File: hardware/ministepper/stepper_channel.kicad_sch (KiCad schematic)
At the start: 14 parts, among them U1 TMC2130-LA

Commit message: ministepper: 0.1 ohm sense resistor LCSC confirmed (C2974119)
Previously marked TBD — UNI-ROYAL FRL1210FR100TS is a 1210 / 1%
100 mOhm sense resistor, LCSC C2974119, ~15k stock, $0.015. Used on
RSA and RSB in the stepper_channel sub-sheet (standard variant).

The DNP micro variant (0.68 ohm 1210, C3000593) stays unchanged.
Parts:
- RSA, RSB: LCSC TBD -> C2974119; MPN RL1220T-R100-F -> FRL1210FR100TS; Manufacturer Yageo -> UNI-ROYAL
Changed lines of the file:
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@@
 		(property "Datasheet" "~" (at 170 155 0) (effects (font (size 1.27 1.27)) hide))
 		(property "Description" "Sense coil A, 0.1 ohm 1% 1210 (standard)" (at 170 155 0) (effects (font (size 1.27 1.27)) hide))
-		(property "LCSC" "TBD" (at 170 155 0) (effects (font (size 1.27 1.27)) hide))
-		(property "MPN" "RL1220T-R100-F" (at 170 155 0) (effects (font (size 1.27 1.27)) hide))
-		(property "Manufacturer" "Yageo" (at 170 155 0) (effects (font (size 1.27 1.27)) hide))
+		(property "LCSC" "C2974119" (at 170 155 0) (effects (font (size 1.27 1.27)) hide))
+		(property "MPN" "FRL1210FR100TS" (at 170 155 0) (effects (font (size 1.27 1.27)) hide))
+		(property "Manufacturer" "UNI-ROYAL" (at 170 155 0) (effects (font (size 1.27 1.27)) hide))
 		(instances (project "ministepper" (path "/e1d2c3b4-a5f6-7890-abcd-ef9876543210/c3d4e5f6-a7b8-9012-cdef-1234567890ab" (reference "RSA") (unit 1))))
 	)
@@
 		(property "Datasheet" "~" (at 175 155 0) (effects (font (size 1.27 1.27)) hide))
 		(property "Description" "Sense coil B, 0.1 ohm 1% 1210 (standard)" (at 175 155 0) (effects (font (size 1.27 1.27)) hide))
-		(property "LCSC" "TBD" (at 175 155 0) (effects (font (size 1.27 1.27)) hide))
-		(property "MPN" "RL1220T-R100-F" (at 175 155 0) (effects (font (size 1.27 1.27)) hide))
-		(property "Manufacturer" "Yageo" (at 175 155 0) (effects (font (size 1.27 1.27)) hide))
+		(property "LCSC" "C2974119" (at 175 155 0) (effects (font (size 1.27 1.27)) hide))
+		(property "MPN" "FRL1210FR100TS" (at 175 155 0) (effects (font (size 1.27 1.27)) hide))
+		(property "Manufacturer" "UNI-ROYAL" (at 175 155 0) (effects (font (size 1.27 1.27)) hide))
 		(instances (project "ministepper" (path "/e1d2c3b4-a5f6-7890-abcd-ef9876543210/c3d4e5f6-a7b8-9012-cdef-1234567890ab" (reference "RSB") (unit 1))))
 	)

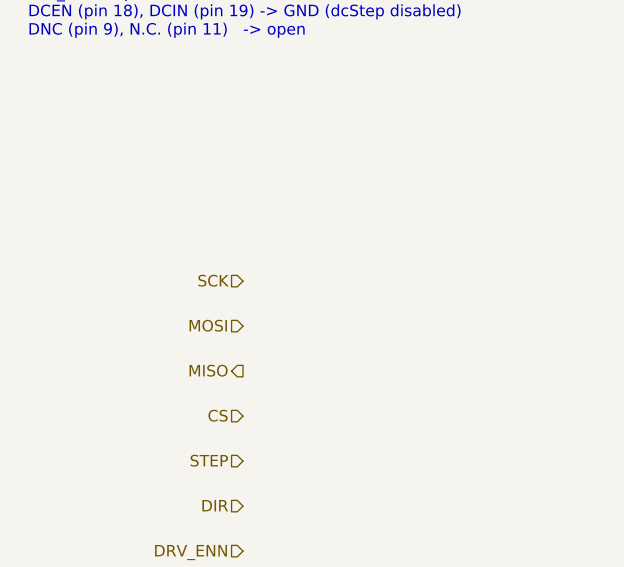
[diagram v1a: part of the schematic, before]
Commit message: ministepper: add (justify left/right) to hier labels and sheet pins
The labels inside stepper_channel.kicad_sch and the sheet-block pins
on the root ministepper.kicad_sch were missing (justify ...) inside
their (effects ...) — which left KiCad to render the text with no
offset from the arrow glyph. User caught it by hand-placing a FOO
hier label in KiCad which came out formatted with (justify left).

Fixed 13 hier labels in the sub-sheet and 24 pins across the two
stepper sheet instances on the root:

  angle 0   (left edge on sub-sheet, or right edge on root sheet) -> justify left
  angle 180 (right edge on sub-sheet, or left edge on root sheet) -> justify right

Text now sits cleanly on the INSIDE side of each pin's triangle glyph
with the standard KiCad offset instead of overlapping the first
letter of each label.
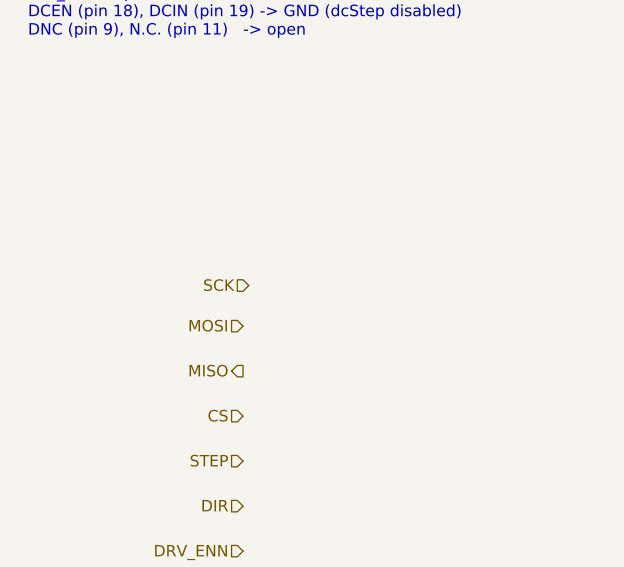
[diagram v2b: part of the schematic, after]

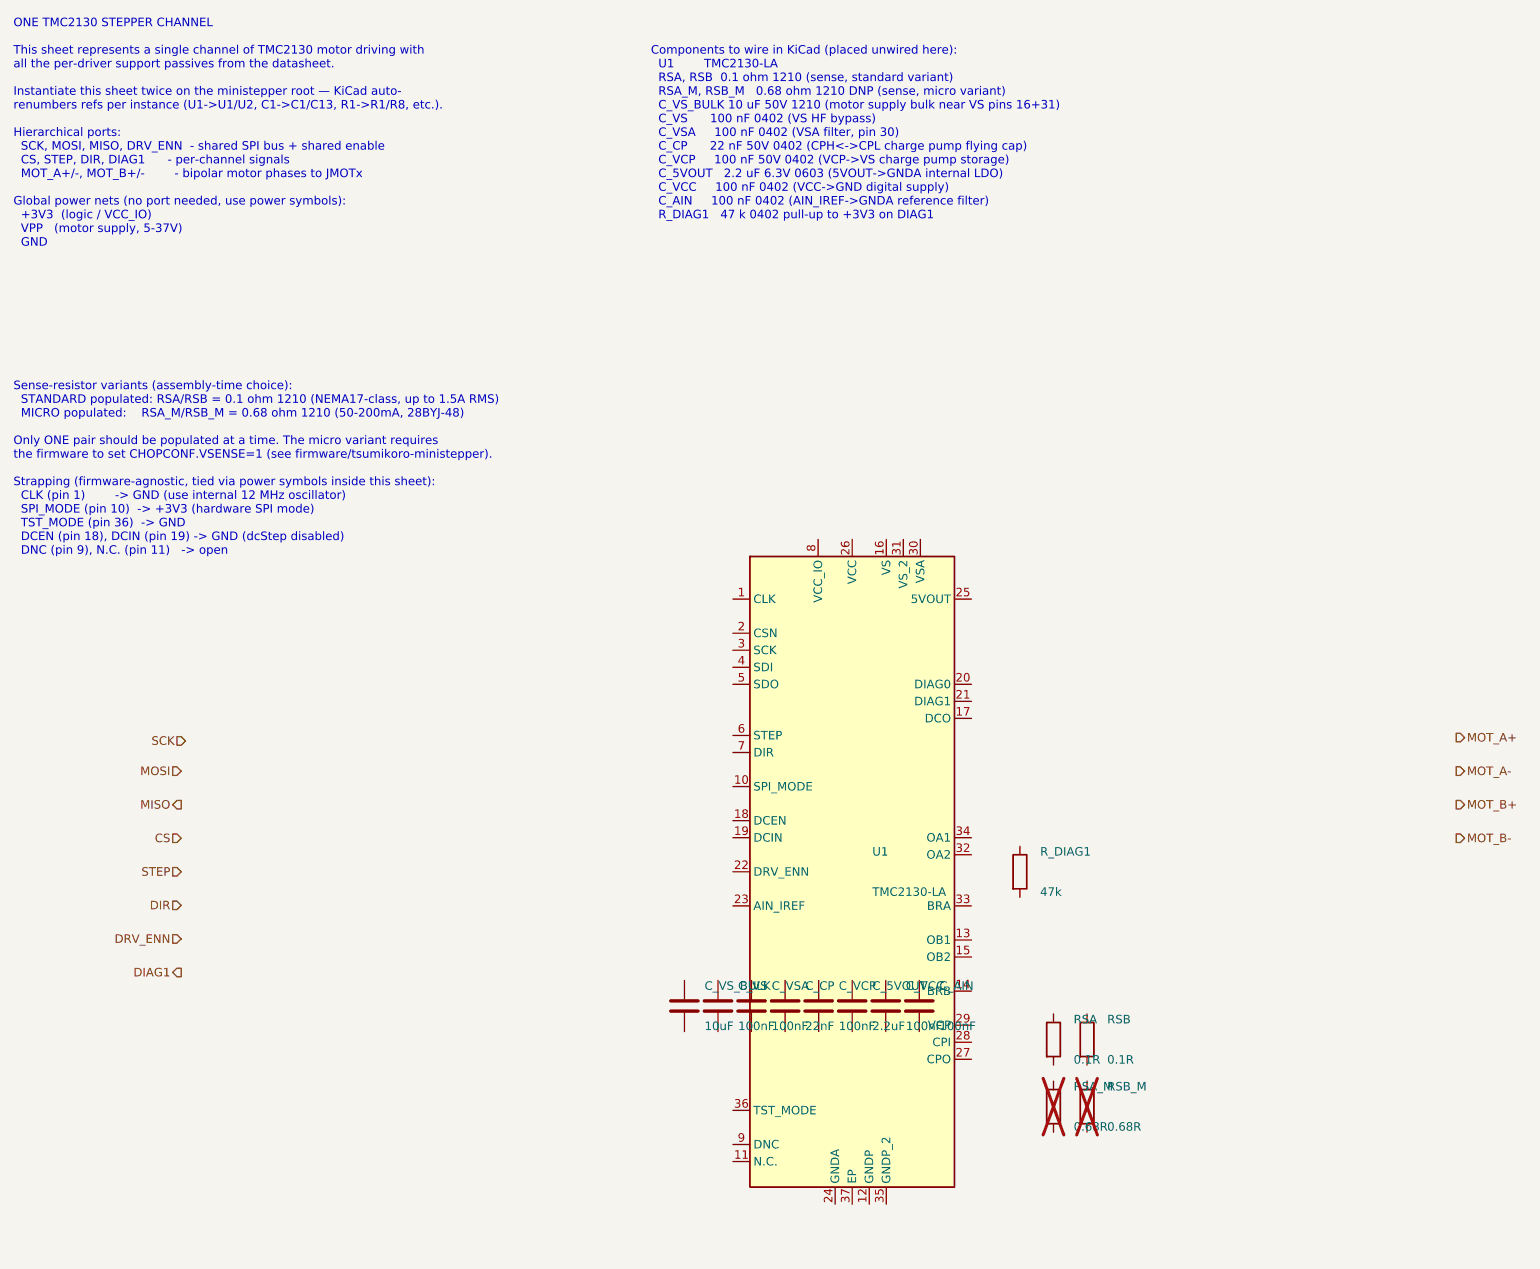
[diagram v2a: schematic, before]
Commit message: ministepper: add BRA/BRB sense-node filter caps
Two new 100 nF 0402 (basic, C1525) caps in stepper_channel.kicad_sch:
  C_BRA_FILT — from BRA (pin 33) to GND, filters switching noise on
               the current-sense node for coil A
  C_BRB_FILT — from BRB (pin 14) to GND, same for coil B

Per the TMC2130 datasheet (fig. 8) and Trinamic app note AN002 these
aren't strictly required but clean up the phase current readback —
especially at higher microstep rates. No harm at lower rates.

Placed near the sense resistors (RSA/RSB) on the sub-sheet. Both
basic JLCPCB parts (same CL05B104KO5NNNC used for the rest of the
100 nF decoupling on this board), so no new BOM line item.
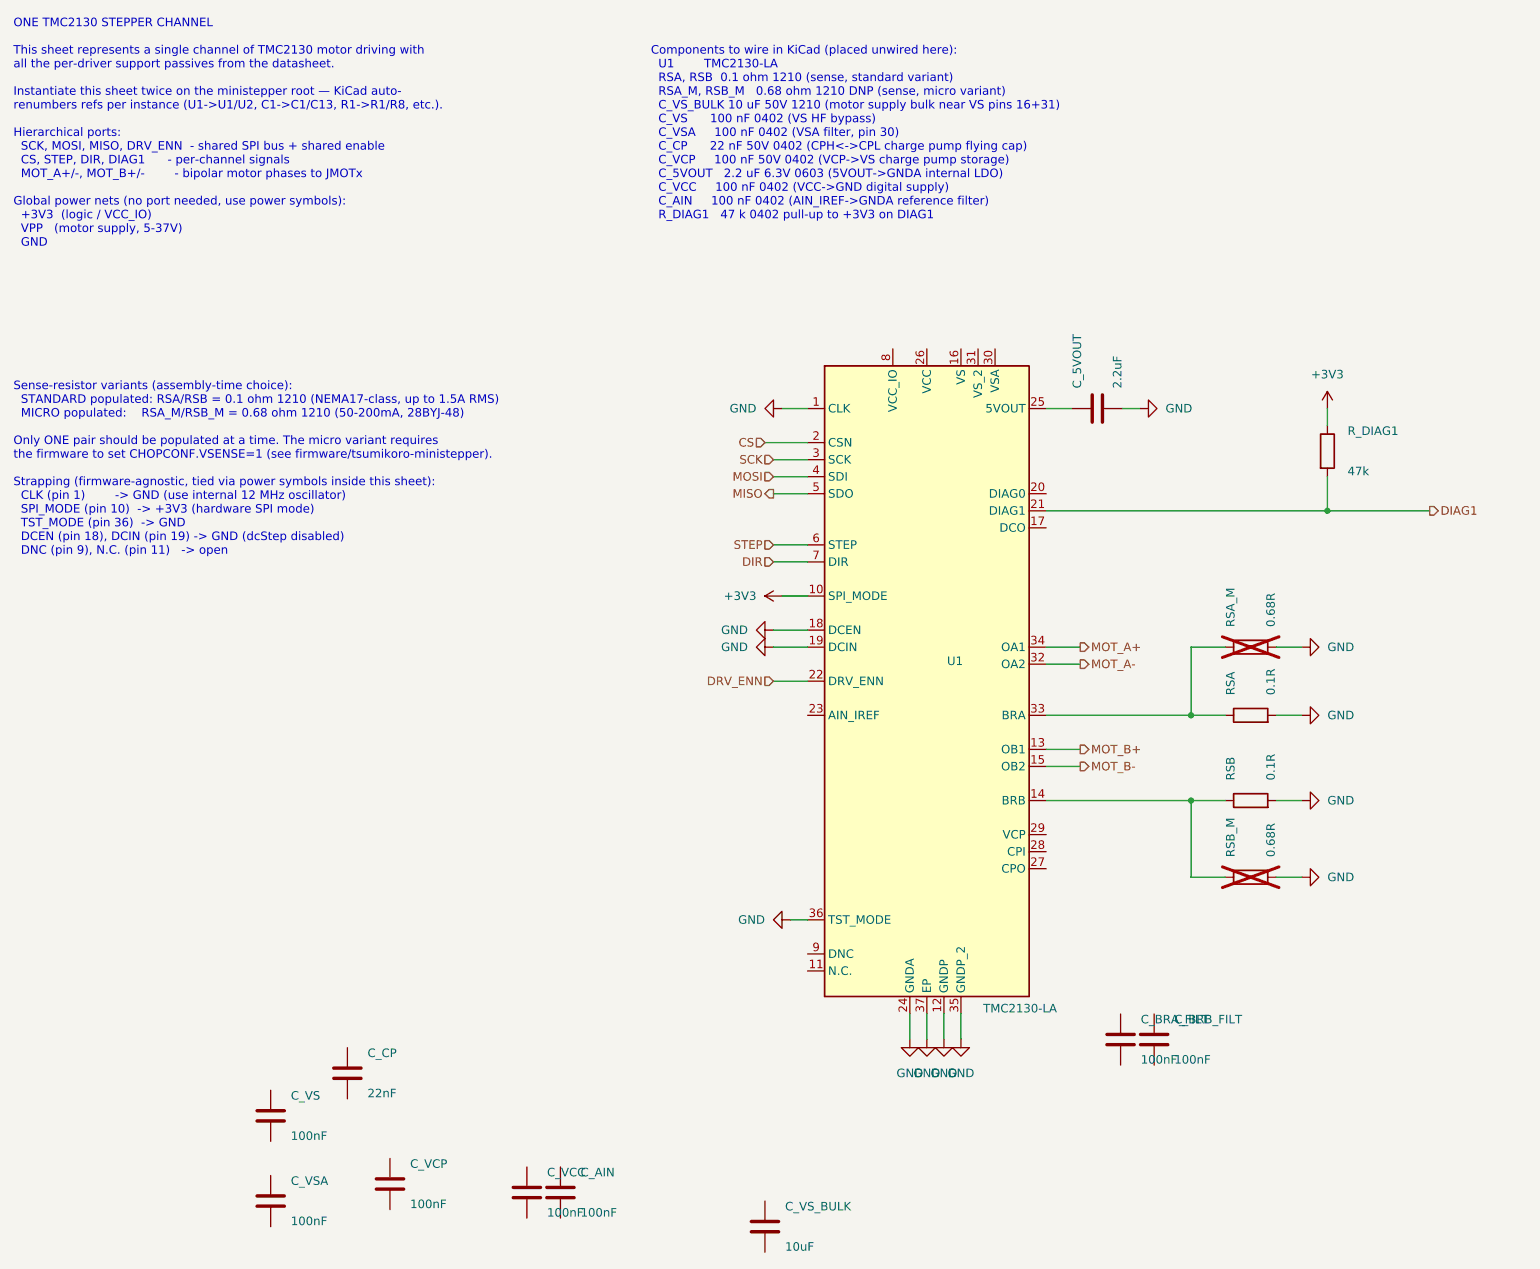
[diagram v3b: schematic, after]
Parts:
- added C_BRA_FILT, C_BRB_FILT: 100nF, Capacitor_SMD:C_0402_1005Metric, symbol Device:C
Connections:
- net CS: now also U1.2 (CSN)
- net DIAG1: now also R_DIAG1.2, U1.21 (DIAG1)
- net DIR: now also U1.7 (DIR)
- net DRV_ENN: now also U1.22 (DRV_ENN)
- net MISO: now also U1.5 (SDO)
- net MOSI: now also U1.4 (SDI)
- net MOT_A+: now also U1.34 (OA1)
- net MOT_A-: now also U1.32 (OA2)
- net MOT_B+: now also U1.13 (OB1)
- net MOT_B-: now also U1.15 (OB2)
- net SCK: now also U1.3 (SCK)
- net STEP: now also U1.6 (STEP)
- net GND: now reaches U1.1 (CLK)
- net GND: now also C_5VOUT.2, RSA.2, RSA_M.2, RSB.2, RSB_M.2, U1.12 (GNDP), U1.18 (DCEN), U1.19 (DCIN), U1.24 (GNDA), U1.35 (GNDP_2), U1.36 (TST_MODE), U1.37 (EP)
- net +3V3: now reaches U1.10 (SPI_MODE)
- net +3V3: now also R_DIAG1.1
- net at U1.14 (BRB): now also RSB.1, RSB_M.1
- net at U1.25 (5VOUT): now also C_5VOUT.1
- net at U1.33 (BRA): now also RSA.1, RSA_M.1
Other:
- moved on the sheet: C_5VOUT, C_AIN, C_CP, C_VCC, C_VCP, C_VS, C_VSA, C_VS_BULK, RSA, RSA_M, RSB, RSB_M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
